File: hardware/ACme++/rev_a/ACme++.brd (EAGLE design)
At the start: 72.6 x 47.1 mm, 92 parts, among them J1 AC-PLUG, J2 TC2030-CTX-NL, J3 WIRE_HOLE-14AWG, J4 WIRE_HOLE-14AWG, J5 WIRE_HOLE-14AWG, K1 S216S01F, Q1 STGD5NB120SZT4, Q2 FDV301N, U1 CC2538, U2 DS2411, U3 FM25LBTDFN-8, U4 ADE7753, U5 TXB0104RGY, U6 SR086SG-G, U7 TDA3664AT, X1 EPSON-FA-128, X2 FC-12M32.7680KA-A3, X3 ECS-35-17-5PX-TR

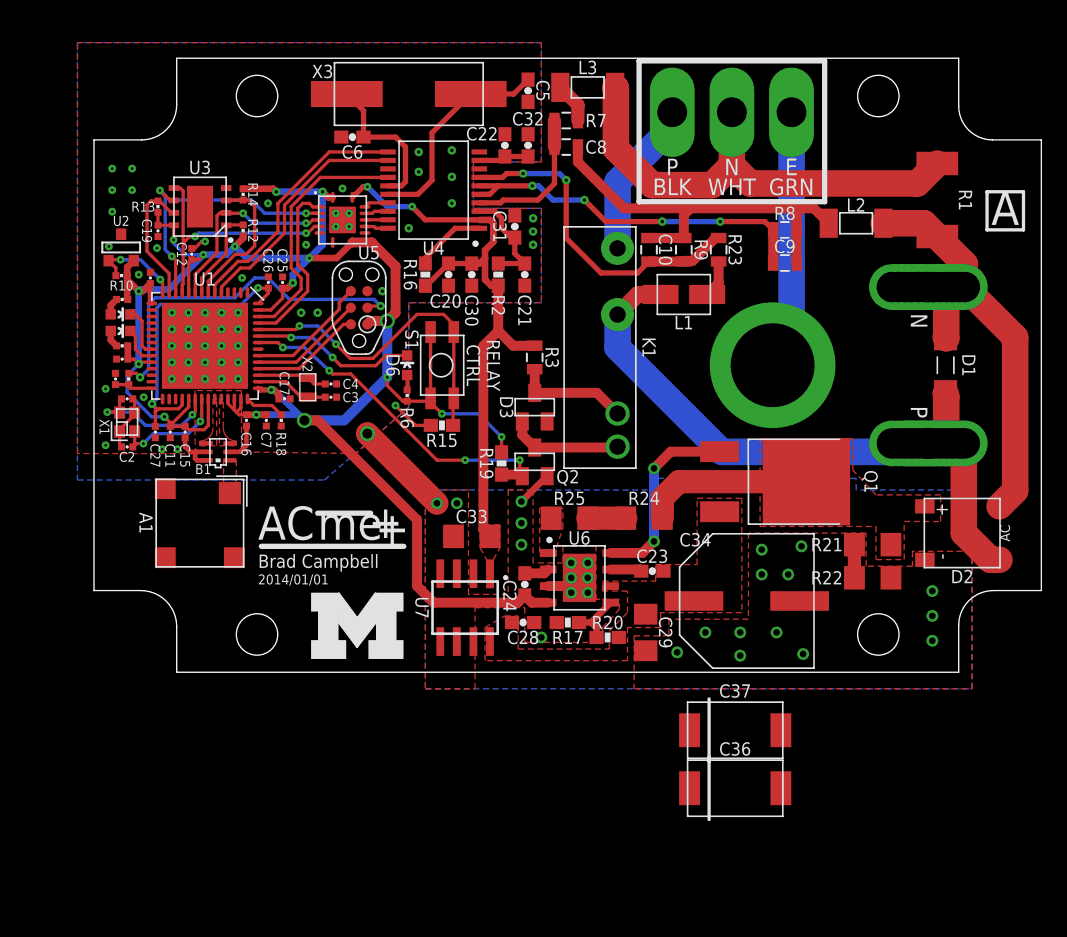
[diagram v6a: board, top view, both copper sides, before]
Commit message: more clearance for phase
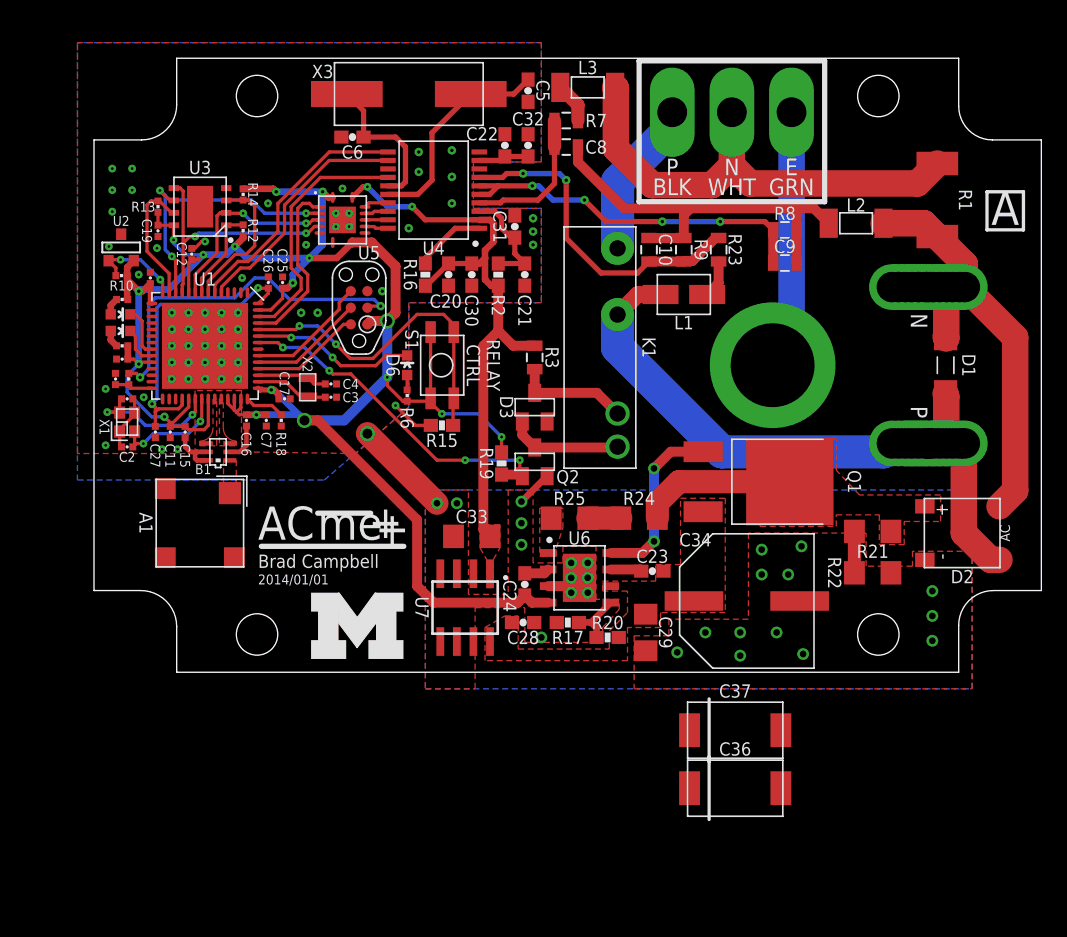
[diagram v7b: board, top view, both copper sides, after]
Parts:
- moved Q1 1.27 mm to (53.3, 14.6)
- moved R21 1.02 mm to (59.7, 10.8)
- moved R22 0.38 mm to (59.7, 7.62)
- moved R24 0.38 mm to (41.8, 11.8)
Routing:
- net SR086_GATE: track 14.8 -> 13.6 mm
- net DC_RECTIFIED: track 13.1 -> 12.0 mm
- net N$18: track 2.54 -> 3.17 mm
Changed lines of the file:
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@@
 <attribute name="VALUE" x="72.698" y="10.668" size="1.016" layer="27" font="vector" ratio="12" rot="R90" align="bottom-center"/>
 </element>
-<element name="R21" library="SparkFun-Resistors" package="1206" value="200k" x="59.69" y="9.779" smashed="yes">
-<attribute name="DIGIKEY" value="P200KALCT-ND" x="59.69" y="9.779" size="1.778" layer="27" display="off"/>
-<attribute name="NAME" x="57.404" y="9.779" size="1.016" layer="25" font="vector" ratio="12" align="center-right"/>
-<attribute name="VALUE" x="58.293" y="8.255" size="0.4064" layer="27"/>
-</element>
-<element name="R22" library="SparkFun-Resistors" package="1206" value="200k" x="59.69" y="7.239" smashed="yes" rot="R180">
-<attribute name="DIGIKEY" value="P200KALCT-ND" x="59.69" y="7.239" size="1.778" layer="27" rot="R180" display="off"/>
-<attribute name="NAME" x="57.404" y="7.239" size="1.016" layer="25" font="vector" ratio="12" align="center-right"/>
-<attribute name="VALUE" x="61.087" y="8.763" size="0.4064" layer="27" rot="R180"/>
-</element>
-<element name="R24" library="SparkFun-Resistors" package="1206" value="510k" x="42.164" y="11.811" smashed="yes">
-<attribute name="DIGIKEY" value="P510KALCT-ND" x="42.164" y="11.811" size="1.778" layer="27" display="off"/>
-<attribute name="NAME" x="42.164" y="12.827" size="1.016" layer="25" font="vector" ratio="12" align="bottom-center"/>
-<attribute name="VALUE" x="40.767" y="10.287" size="0.4064" layer="27"/>
+<element name="R21" library="SparkFun-Resistors" package="1206" value="200k" x="59.69" y="10.795" smashed="yes">
+<attribute name="DIGIKEY" value="P200KALCT-ND" x="59.69" y="10.795" size="1.778" layer="27" display="off"/>
+<attribute name="NAME" x="59.69" y="9.779" size="1.016" layer="25" font="vector" ratio="12" align="top-center"/>
+<attribute name="VALUE" x="58.293" y="9.271" size="0.4064" layer="27"/>
+</element>
+<element name="R22" library="SparkFun-Resistors" package="1206" value="200k" x="59.69" y="7.62" smashed="yes" rot="R180">
+<attribute name="DIGIKEY" value="P200KALCT-ND" x="59.69" y="7.62" size="1.778" layer="27" rot="R180" display="off"/>
+<attribute name="NAME" x="57.277" y="7.62" size="1.016" layer="25" font="vector" ratio="12" rot="SR270" align="top-center"/>
+<attribute name="VALUE" x="61.087" y="9.144" size="0.4064" layer="27" rot="R180"/>
+</element>
+<element name="R24" library="SparkFun-Resistors" package="1206" value="510k" x="41.783" y="11.811" smashed="yes">
+<attribute name="DIGIKEY" value="P510KALCT-ND" x="41.783" y="11.811" size="1.778" layer="27" display="off"/>
+<attribute name="NAME" x="41.783" y="12.827" size="1.016" layer="25" font="vector" ratio="12" align="bottom-center"/>
+<attribute name="VALUE" x="40.386" y="10.287" size="0.4064" layer="27"/>
 </element>
 <element name="R25" library="SparkFun-Resistors" package="1206" value="510k" x="36.449" y="11.811" smashed="yes">
@@
 <attribute name="VALUE" x="35.052" y="10.287" size="0.4064" layer="27"/>
 </element>
-<element name="Q1" library="powercube" package="DPAK" value="STGD5NB120SZT4" x="54.61" y="14.605" smashed="yes" rot="R270">
-<attribute name="DIGIKEY" value="497-4352-1-ND" x="54.61" y="14.605" size="1.778" layer="27" rot="R270" display="off"/>
-<attribute name="NAME" x="59.055" y="14.605" size="1.016" layer="25" font="vector" ratio="12" rot="SR270" align="bottom-center"/>
-<attribute name="VALUE" x="44.45" y="14.605" size="1.016" layer="27" font="vector" ratio="12" rot="R270" align="bottom-center"/>
+<element name="Q1" library="powercube" package="DPAK" value="STGD5NB120SZT4" x="53.34" y="14.605" smashed="yes" rot="R270">
+<attribute name="DIGIKEY" value="497-4352-1-ND" x="53.34" y="14.605" size="1.778" layer="27" rot="R270" display="off"/>
+<attribute name="NAME" x="57.785" y="14.605" size="1.016" layer="25" font="vector" ratio="12" rot="SR270" align="bottom-center"/>
+<attribute name="VALUE" x="43.18" y="14.605" size="1.016" layer="27" font="vector" ratio="12" rot="R270" align="bottom-center"/>
 </element>
 <element name="C29" library="SparkFun-Passives" package="1206" value="1uF" x="42.291" y="3.048" smashed="yes" rot="R270">
@@
 <vertex x="67.31" y="-1.27"/>
 <vertex x="67.31" y="13.97"/>
-<vertex x="58.42" y="13.97"/>
-<vertex x="58.42" y="14.859"/>
-<vertex x="43.18" y="14.859"/>
-<vertex x="43.18" y="13.97"/>
 <vertex x="25.4" y="13.97"/>
 <vertex x="25.4" y="-1.27"/>
@@
 <wire x1="66.3448" y1="17.5387" x2="66.7512" y2="17.5387" width="0.254" layer="1"/>
 <contactref element="K1" pad="2"/>
-<wire x1="61.1632" y1="17.5387" x2="60.5155" y2="16.891" width="2.032" layer="16"/>
-<wire x1="60.5155" y1="16.891" x2="48.133" y2="16.891" width="2.032" layer="16"/>
-<wire x1="48.133" y1="16.891" x2="40.132" y2="24.892" width="2.032" layer="16"/>
-<wire x1="40.132" y1="24.892" x2="40.132" y2="27.414" width="2.032" layer="16"/>
+<wire x1="61.1632" y1="17.5387" x2="60.5155" y2="16.891" width="2.54" layer="16"/>
+<wire x1="60.5155" y1="16.891" x2="48.133" y2="16.891" width="2.54" layer="16"/>
+<wire x1="48.133" y1="16.891" x2="40.132" y2="24.892" width="2.54" layer="16"/>
+<wire x1="40.132" y1="24.892" x2="40.132" y2="27.414" width="2.54" layer="16"/>
 <wire x1="40.132" y1="27.414" x2="41.674" y2="28.956" width="1.27" layer="1"/>
 <wire x1="41.674" y1="28.956" x2="43.4213" y2="28.956" width="1.27" layer="1"/>
@@
 <contactref element="J3" pad="P$1"/>
 <contactref element="K1" pad="1"/>
-<wire x1="40.132" y1="32.494" x2="40.132" y2="37.592" width="2.032" layer="16"/>
-<wire x1="40.132" y1="37.592" x2="44.323" y2="41.783" width="2.032" layer="16"/>
-<wire x1="44.323" y1="41.783" x2="44.323" y2="42.926" width="2.032" layer="16"/>
+<wire x1="40.132" y1="32.494" x2="40.132" y2="37.592" width="2.54" layer="16"/>
+<wire x1="40.132" y1="37.592" x2="44.323" y2="41.783" width="2.54" layer="16"/>
+<wire x1="44.323" y1="41.783" x2="44.323" y2="42.926" width="2.54" layer="16"/>
 </signal>
 <signal name="WALL_NEUTRAL_EMI">
@@
 <polygon width="0.254" layer="1" thermals="no">
 <vertex x="64.897" y="13.589"/>
-<vertex x="59.944" y="13.589"/>
-<vertex x="58.166" y="15.494"/>
-<vertex x="58.166" y="17.907"/>
+<vertex x="58.674" y="13.589"/>
+<vertex x="56.896" y="15.494"/>
+<vertex x="56.896" y="17.907"/>
 <vertex x="51.054" y="17.907"/>
 <vertex x="51.054" y="11.176"/>
-<vertex x="59.944" y="11.176"/>
-<vertex x="59.944" y="8.636"/>
-<vertex x="62.103" y="8.636"/>
+<vertex x="56.896" y="11.176"/>
+<vertex x="56.896" y="12.065"/>
+<vertex x="60.198" y="12.065"/>
+<vertex x="60.198" y="9.779"/>
+<vertex x="62.103" y="9.779"/>
 <vertex x="62.103" y="11.557"/>
 <vertex x="64.897" y="11.557"/>
 </polygon>
-<wire x1="54.61" y1="14.605" x2="44.831" y2="14.605" width="1.778" layer="1"/>
-<wire x1="44.831" y1="14.605" x2="43.564" y2="13.338" width="1.778" layer="1"/>
-<wire x1="43.564" y1="13.338" x2="43.564" y2="11.811" width="1.778" layer="1"/>
+<wire x1="53.34" y1="14.605" x2="44.831" y2="14.605" width="1.778" layer="1"/>
+<wire x1="44.831" y1="14.605" x2="43.183" y2="12.957" width="1.778" layer="1"/>
+<wire x1="43.183" y1="12.957" x2="43.183" y2="11.811" width="1.778" layer="1"/>
 </signal>
 <signal name="N$18">
 <contactref element="R21" pad="1"/>
 <contactref element="R22" pad="2"/>
-<wire x1="58.29" y1="9.779" x2="58.29" y2="7.239" width="1.016" layer="1"/>
+<wire x1="58.29" y1="10.795" x2="58.29" y2="7.62" width="1.016" layer="1"/>
 </signal>
 <signal name="N$21">
 <contactref element="R25" pad="2"/>
 <contactref element="R24" pad="1"/>
-<wire x1="40.764" y1="11.811" x2="37.849" y2="11.811" width="1.778" layer="1"/>
+<wire x1="40.383" y1="11.811" x2="37.849" y2="11.811" width="1.778" layer="1"/>
 </signal>
 <signal name="SR086_VIN">
@@
 <contactref element="U6" pad="8"/>
 <via x="42.926" y="15.621" extent="1-16" drill="0.508"/>
-<wire x1="47.96" y1="16.905" x2="44.21" y2="16.905" width="0.762" layer="1"/>
+<wire x1="46.69" y1="16.905" x2="44.21" y2="16.905" width="0.762" layer="1"/>
 <wire x1="44.21" y1="16.905" x2="42.926" y2="15.621" width="0.762" layer="1"/>
 <wire x1="42.926" y1="15.621" x2="42.926" y2="10.033" width="0.762" layer="16"/>
@@
 <contactref element="C28" pad="1"/>
 <polygon width="0.254" layer="1" thermals="no">
-<vertex x="49.657" y="13.335"/>
-<vertex x="49.657" y="4.572"/>
+<vertex x="48.387" y="13.335"/>
+<vertex x="48.387" y="4.572"/>
 <vertex x="43.434" y="4.572"/>
 <vertex x="43.434" y="3.429"/>
@@
 <vertex x="43.053" y="6.985"/>
 <vertex x="43.053" y="8.255"/>
-<vertex x="46.228" y="8.255"/>
-<vertex x="46.228" y="13.335"/>
+<vertex x="44.958" y="8.255"/>
+<vertex x="44.958" y="13.335"/>
 </polygon>
 </signal>
